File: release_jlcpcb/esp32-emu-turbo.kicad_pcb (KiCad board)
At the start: 4 copper layers, 160 x 75 mm, 71 parts, among them J1 USB-C-16P, J3 JST-PH-2P, J4 FPC-40P-0.5mm, SW1 SW-SMD-5.1x5.1, SW10 SW-SMD-5.1x5.1, SW11 SW-SMD-5.1x5.1, SW12 SW-SMD-5.1x5.1, SW13 SW-SMD-5.1x5.1, SW2 SW-SMD-5.1x5.1, SW3 SW-SMD-5.1x5.1, SW4 SW-SMD-5.1x5.1, SW5 SW-SMD-5.1x5.1, SW6 SW-SMD-5.1x5.1, SW7 SW-SMD-5.1x5.1, SW8 SW-SMD-5.1x5.1, SW9 SW-SMD-5.1x5.1, U1 ESP32-S3-WROOM-1-N16R8, U2 ESOP-8, U3 SOT-223, U5 SOP-16, U6 TF-01A

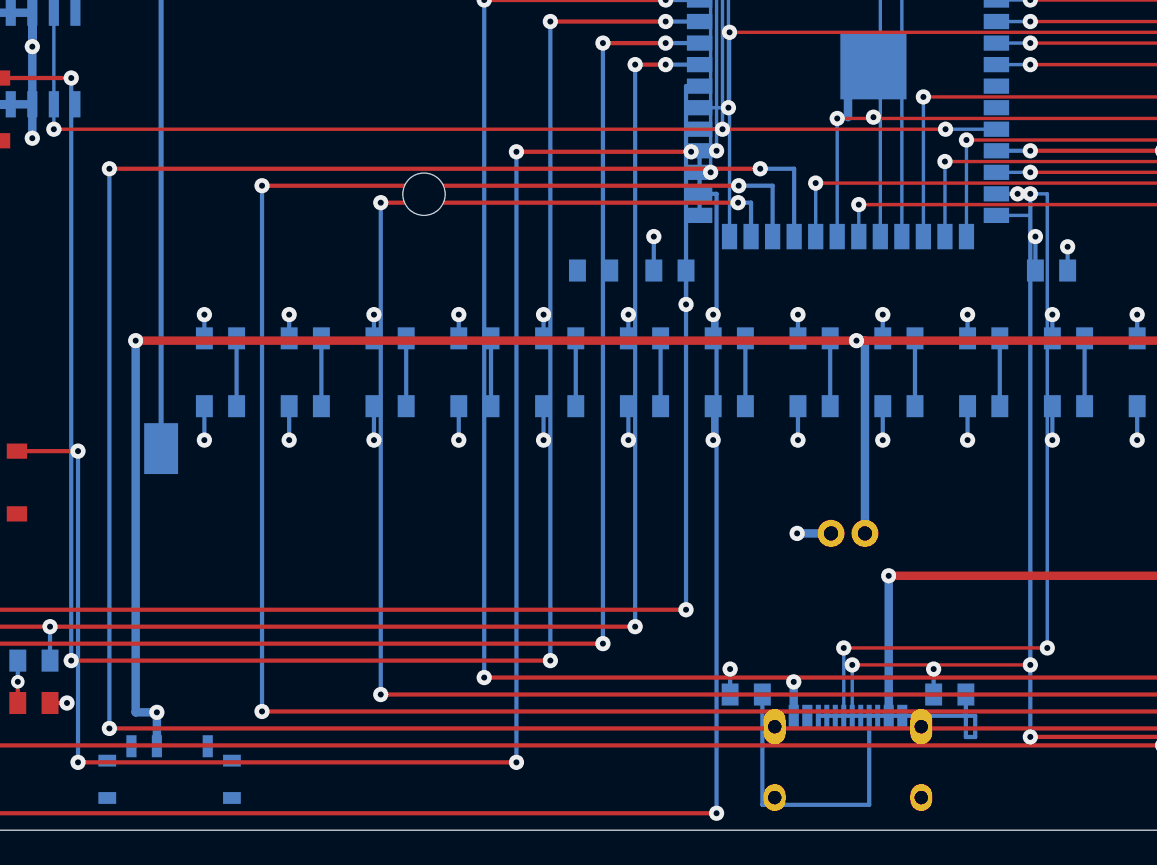
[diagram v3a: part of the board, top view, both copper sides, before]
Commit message: Fix 4 JLCPCB DFM DANGER violations: USB trace spacing, button via/MH clearance
- USB D+/D- B.Cu columns shifted inward (dp_col_x +1.5, dm_col_x +2.5) to
  clear GND cap traces (gap 0.575mm, was 0.075mm)
- Button stagger_y lowered to 35.5 (was 38.0) to clear MH(55,37.5) drill zone
- Button near_epx vias staggered with 0.4mm offset to separate BTN_B/BTN_X
  via pair (pad gap 0.177mm, was 0.101mm)
- Added 2 DFM guard tests: USB cap trace spacing + MH trace clearance (41/41)
- Regenerated gerbers with zone fill + updated release_jlcpcb + SVG renders

Co-Authored-By: Claude Opus 4.6 <noreply@anthropic.com>
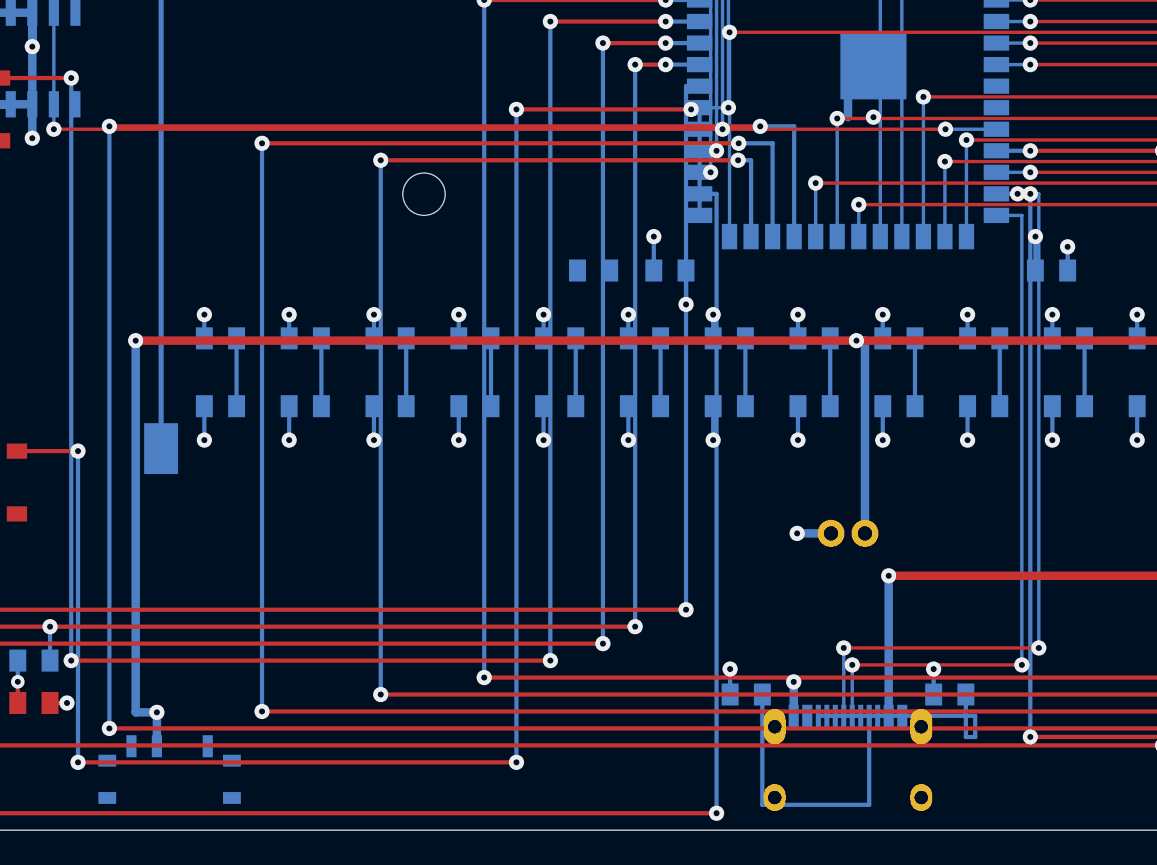
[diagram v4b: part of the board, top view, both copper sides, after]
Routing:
- net BTN_Y: track 213.9 -> 218.9 mm
- net BTN_X: track 189.0 -> 194.0 mm
- net BTN_SELECT: track 102.3 -> 107.3 mm
- net BTN_B: track 189.7 -> 194.7 mm
- net USB_D-: track 45.8 -> 44.8 mm
- net USB_D+: track 42.0 -> 41.0 mm
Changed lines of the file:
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@@
   (segment (start 80.25 68.255) (end 80.25 65.255) (width 0.2) (layer "B.Cu") (net 40))
   (via (at 80.25 65.255) (size 0.9) (drill 0.35) (layers "F.Cu" "B.Cu") (net 40))
-  (segment (start 80.25 65.255) (end 90.75 65.255) (width 0.2) (layer "F.Cu") (net 40))
-  (via (at 90.75 65.255) (size 0.9) (drill 0.35) (layers "F.Cu" "B.Cu") (net 40))
-  (segment (start 90.75 65.255) (end 90.75 38.75) (width 0.2) (layer "B.Cu") (net 40))
-  (segment (start 90.75 38.75) (end 88.75 38.75) (width 0.2) (layer "B.Cu") (net 40))
+  (segment (start 80.25 65.255) (end 90.25 65.255) (width 0.2) (layer "F.Cu") (net 40))
+  (via (at 90.25 65.255) (size 0.9) (drill 0.35) (layers "F.Cu" "B.Cu") (net 40))
+  (segment (start 90.25 65.255) (end 90.25 38.75) (width 0.2) (layer "B.Cu") (net 40))
+  (segment (start 90.25 38.75) (end 88.75 38.75) (width 0.2) (layer "B.Cu") (net 40))
   (segment (start 79.75 68.255) (end 79.75 64.255) (width 0.2) (layer "B.Cu") (net 41))
   (via (at 79.75 64.255) (size 0.9) (drill 0.35) (layers "F.Cu" "B.Cu") (net 41))
-  (segment (start 79.75 64.255) (end 91.75 64.255) (width 0.2) (layer "F.Cu") (net 41))
-  (via (at 91.75 64.255) (size 0.9) (drill 0.35) (layers "F.Cu" "B.Cu") (net 41))
-  (segment (start 91.75 64.255) (end 91.75 37.480000000000004) (width 0.2) (layer "B.Cu") (net 41))
-  (segment (start 91.75 37.480000000000004) (end 88.75 37.480000000000004) (width 0.2) (layer "B.Cu") (net 41))
+  (segment (start 79.75 64.255) (end 91.25 64.255) (width 0.2) (layer "F.Cu") (net 41))
+  (via (at 91.25 64.255) (size 0.9) (drill 0.35) (layers "F.Cu" "B.Cu") (net 41))
+  (segment (start 91.25 64.255) (end 91.25 37.480000000000004) (width 0.2) (layer "B.Cu") (net 41))
+  (segment (start 91.25 37.480000000000004) (end 88.75 37.480000000000004) (width 0.2) (layer "B.Cu") (net 41))
   (segment (start 78.25 68.255) (end 87.5 68.255) (width 0.25) (layer "B.Cu") (net 49))
   (segment (start 87.5 68.255) (end 87.5 69.505) (width 0.25) (layer "B.Cu") (net 49))
@@
   (segment (start 131.4 67.0) (end 52.45 67.0) (width 0.25) (layer "F.Cu") (net 32))
   (via (at 52.45 67.0) (size 0.9) (drill 0.35) (layers "F.Cu" "B.Cu") (net 32))
-  (segment (start 52.45 67.0) (end 52.45 38.0) (width 0.25) (layer "B.Cu") (net 32))
-  (via (at 52.45 38.0) (size 0.9) (drill 0.35) (layers "F.Cu" "B.Cu") (net 32))
-  (segment (start 52.45 38.0) (end 73.52 38.0) (width 0.25) (layer "F.Cu") (net 32))
-  (via (at 73.52 38.0) (size 0.9) (drill 0.35) (layers "F.Cu" "B.Cu") (net 32))
-  (segment (start 73.52 38.0) (end 74.285 38.0) (width 0.25) (layer "B.Cu") (net 32))
-  (segment (start 74.285 38.0) (end 74.285 40.0) (width 0.25) (layer "B.Cu") (net 32))
+  (segment (start 52.45 67.0) (end 52.45 35.5) (width 0.25) (layer "B.Cu") (net 32))
+  (via (at 52.45 35.5) (size 0.9) (drill 0.35) (layers "F.Cu" "B.Cu") (net 32))
+  (segment (start 52.45 35.5) (end 73.52 35.5) (width 0.25) (layer "F.Cu") (net 32))
+  (via (at 73.52 35.5) (size 0.9) (drill 0.35) (layers "F.Cu" "B.Cu") (net 32))
+  (segment (start 73.52 35.5) (end 74.285 35.5) (width 0.25) (layer "B.Cu") (net 32))
+  (segment (start 74.285 35.5) (end 74.285 40.0) (width 0.25) (layer "B.Cu") (net 32))
   (segment (start 155.0 34.35) (end 153.5 34.35) (width 0.25) (layer "F.Cu") (net 1))
   (segment (start 153.5 34.35) (end 153.5 34.85) (width 0.25) (layer "F.Cu") (net 1))
@@
   (segment (start 131.0 68.0) (end 45.45 68.0) (width 0.25) (layer "F.Cu") (net 33))
   (via (at 45.45 68.0) (size 0.9) (drill 0.35) (layers "F.Cu" "B.Cu") (net 33))
-  (segment (start 45.45 68.0) (end 45.45 37.0) (width 0.25) (layer "B.Cu") (net 33))
-  (via (at 45.45 37.0) (size 0.9) (drill 0.35) (layers "F.Cu" "B.Cu") (net 33))
-  (segment (start 45.45 37.0) (end 73.555 37.0) (width 0.25) (layer "F.Cu") (net 33))
-  (via (at 73.555 37.0) (size 0.9) (drill 0.35) (layers "F.Cu" "B.Cu") (net 33))
-  (segment (start 73.555 37.0) (end 75.555 37.0) (width 0.25) (layer "B.Cu") (net 33))
-  (segment (start 75.555 37.0) (end 75.555 40.0) (width 0.25) (layer "B.Cu") (net 33))
+  (segment (start 45.45 68.0) (end 45.45 34.5) (width 0.25) (layer "B.Cu") (net 33))
+  (via (at 45.45 34.5) (size 0.9) (drill 0.35) (layers "F.Cu" "B.Cu") (net 33))
+  (segment (start 45.45 34.5) (end 73.555 34.5) (width 0.25) (layer "F.Cu") (net 33))
+  (via (at 73.555 34.5) (size 0.9) (drill 0.35) (layers "F.Cu" "B.Cu") (net 33))
+  (segment (start 73.555 34.5) (end 75.555 34.5) (width 0.25) (layer "B.Cu") (net 33))
+  (segment (start 75.555 34.5) (end 75.555 40.0) (width 0.25) (layer "B.Cu") (net 33))
   (segment (start 145.0 44.35) (end 143.5 44.35) (width 0.25) (layer "F.Cu") (net 1))
   (segment (start 143.5 44.35) (end 143.5 44.85) (width 0.25) (layer "F.Cu") (net 1))
@@
   (segment (start 130.29999999999998 69.0) (end 36.45 69.0) (width 0.25) (layer "F.Cu") (net 34))
   (via (at 36.45 69.0) (size 0.9) (drill 0.35) (layers "F.Cu" "B.Cu") (net 34))
-  (segment (start 36.45 69.0) (end 36.45 36.0) (width 0.25) (layer "B.Cu") (net 34))
-  (via (at 36.45 36.0) (size 0.9) (drill 0.35) (layers "F.Cu" "B.Cu") (net 34))
-  (segment (start 36.45 36.0) (end 74.825 36.0) (width 0.25) (layer "F.Cu") (net 34))
-  (via (at 74.825 36.0) (size 0.9) (drill 0.35) (layers "F.Cu" "B.Cu") (net 34))
-  (segment (start 74.825 36.0) (end 76.825 36.0) (width 0.25) (layer "B.Cu") (net 34))
-  (segment (start 76.825 36.0) (end 76.825 40.0) (width 0.25) (layer "B.Cu") (net 34))
+  (segment (start 36.45 69.0) (end 36.45 33.5) (width 0.25) (layer "B.Cu") (net 34))
+  (via (at 36.45 33.5) (size 0.9) (drill 0.35) (layers "F.Cu" "B.Cu") (net 34))
+  (segment (start 36.45 33.5) (end 74.825 33.5) (width 0.25) (layer "F.Cu") (net 34))
+  (via (at 74.825 33.5) (size 0.9) (drill 0.35) (layers "F.Cu" "B.Cu") (net 34))
+  (segment (start 74.825 33.5) (end 76.825 33.5) (width 0.25) (layer "B.Cu") (net 34))
+  (segment (start 76.825 33.5) (end 76.825 40.0) (width 0.25) (layer "B.Cu") (net 34))
   (segment (start 136.0 34.35) (end 134.5 34.35) (width 0.25) (layer "F.Cu") (net 1))
   (segment (start 134.5 34.35) (end 134.5 34.85) (width 0.25) (layer "F.Cu") (net 1))
@@
   (segment (start 34.6 71.0) (end 60.45 71.0) (width 0.25) (layer "F.Cu") (net 36))
   (via (at 60.45 71.0) (size 0.9) (drill 0.35) (layers "F.Cu" "B.Cu") (net 36))
-  (segment (start 60.45 71.0) (end 60.45 35.0) (width 0.25) (layer "B.Cu") (net 36))
-  (via (at 60.45 35.0) (size 0.9) (drill 0.35) (layers "F.Cu" "B.Cu") (net 36))
-  (segment (start 60.45 35.0) (end 70.75 35.0) (width 0.25) (layer "F.Cu") (net 36))
-  (via (at 70.75 35.0) (size 0.9) (drill 0.35) (layers "F.Cu" "B.Cu") (net 36))
-  (segment (start 70.75 35.0) (end 71.25 35.0) (width 0.25) (layer "B.Cu") (net 36))
-  (segment (start 71.25 35.0) (end 71.25 38.75) (width 0.25) (layer "B.Cu") (net 36))
+  (segment (start 60.45 71.0) (end 60.45 32.5) (width 0.25) (layer "B.Cu") (net 36))
+  (via (at 60.45 32.5) (size 0.9) (drill 0.35) (layers "F.Cu" "B.Cu") (net 36))
+  (segment (start 60.45 32.5) (end 70.75 32.5) (width 0.25) (layer "F.Cu") (net 36))
+  (via (at 70.75 32.5) (size 0.9) (drill 0.35) (layers "F.Cu" "B.Cu") (net 36))
+  (segment (start 70.75 32.5) (end 71.25 32.5) (width 0.25) (layer "B.Cu") (net 36))
+  (segment (start 71.25 32.5) (end 71.25 38.75) (width 0.25) (layer "B.Cu") (net 36))
   (segment (start 25.0 56.35) (end 26.5 56.35) (width 0.25) (layer "F.Cu") (net 1))
   (segment (start 26.5 56.35) (end 26.5 56.85) (width 0.25) (layer "F.Cu") (net 1))

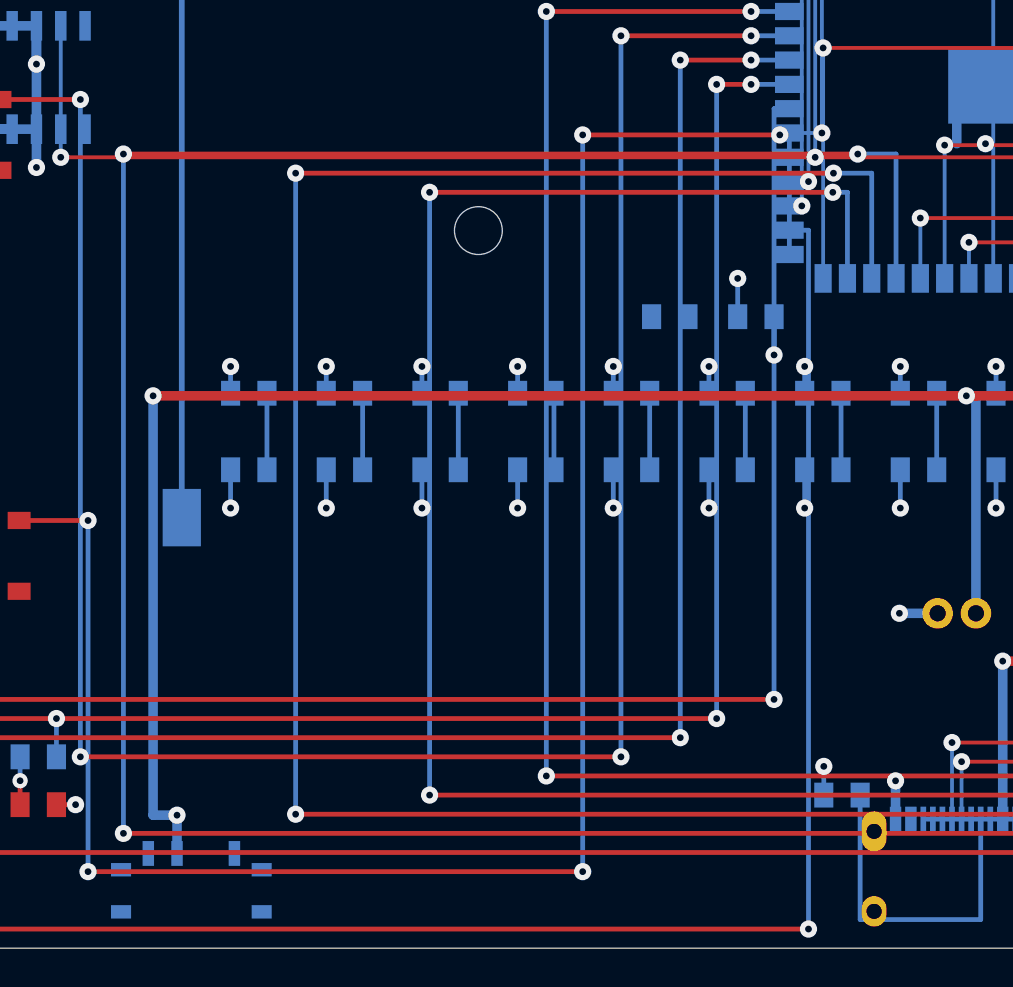
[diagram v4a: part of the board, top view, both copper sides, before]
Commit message: Fix last 2 JLCPCB DFM DANGER: button stagger via pad spacing
- Increased button stagger Y step from 1.0mm to 1.2mm to separate
  BTN_A/BTN_X via pair (pad gap 0.30mm, was 0.10mm DANGER)
- Both F.Cu and B.Cu pad spacing dangers resolved (same via pair)
- 41/41 DFM tests pass, trace spacing improved to 16 (baseline 27)
- Regenerated gerbers + release_jlcpcb + SVG renders

Co-Authored-By: Claude Opus 4.6 <noreply@anthropic.com>
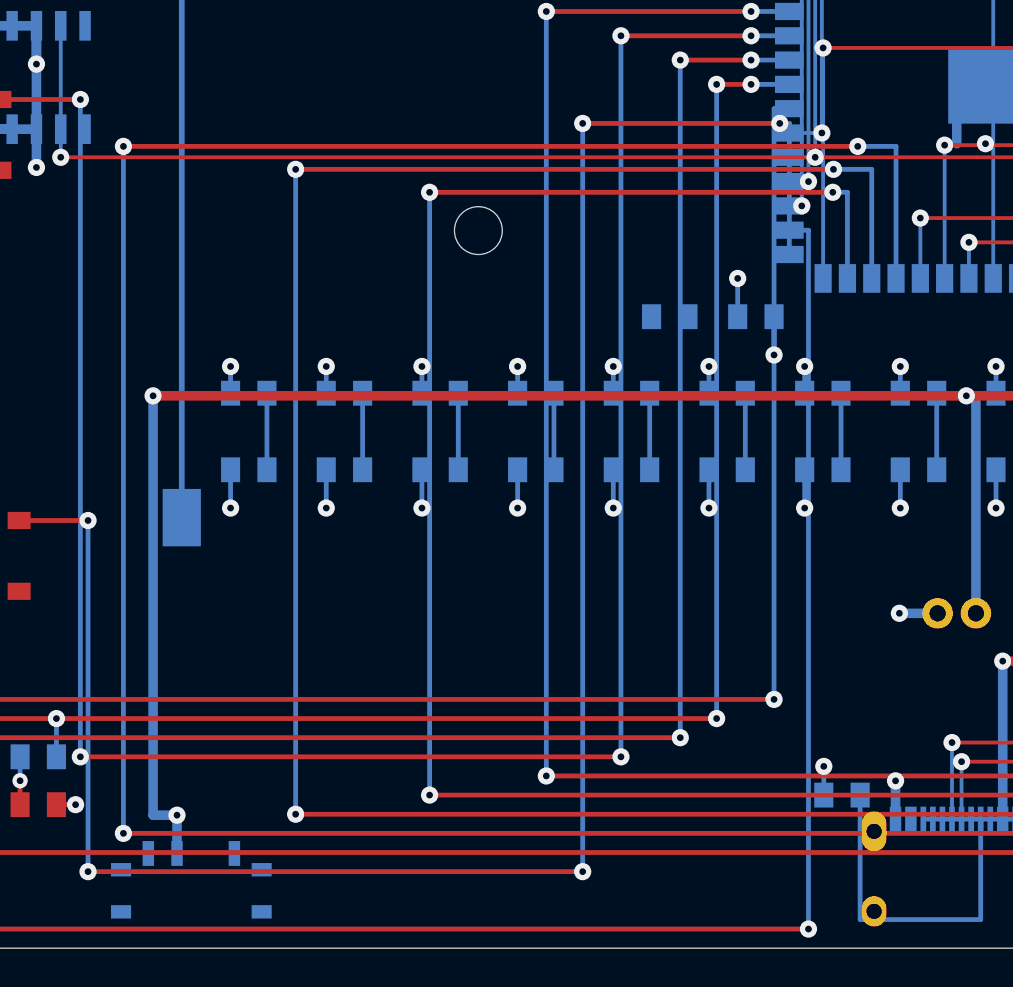
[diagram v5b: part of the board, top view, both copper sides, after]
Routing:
- net BTN_SELECT: track 107.3 -> 108.6 mm
- net BTN_Y: track 218.9 -> 219.7 mm
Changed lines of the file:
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@@
   (segment (start 131.0 68.0) (end 45.45 68.0) (width 0.25) (layer "F.Cu") (net 33))
   (via (at 45.45 68.0) (size 0.9) (drill 0.35) (layers "F.Cu" "B.Cu") (net 33))
-  (segment (start 45.45 68.0) (end 45.45 34.5) (width 0.25) (layer "B.Cu") (net 33))
-  (via (at 45.45 34.5) (size 0.9) (drill 0.35) (layers "F.Cu" "B.Cu") (net 33))
-  (segment (start 45.45 34.5) (end 73.555 34.5) (width 0.25) (layer "F.Cu") (net 33))
-  (via (at 73.555 34.5) (size 0.9) (drill 0.35) (layers "F.Cu" "B.Cu") (net 33))
-  (segment (start 73.555 34.5) (end 75.555 34.5) (width 0.25) (layer "B.Cu") (net 33))
-  (segment (start 75.555 34.5) (end 75.555 40.0) (width 0.25) (layer "B.Cu") (net 33))
+  (segment (start 45.45 68.0) (end 45.45 34.3) (width 0.25) (layer "B.Cu") (net 33))
+  (via (at 45.45 34.3) (size 0.9) (drill 0.35) (layers "F.Cu" "B.Cu") (net 33))
+  (segment (start 45.45 34.3) (end 73.555 34.3) (width 0.25) (layer "F.Cu") (net 33))
+  (via (at 73.555 34.3) (size 0.9) (drill 0.35) (layers "F.Cu" "B.Cu") (net 33))
+  (segment (start 73.555 34.3) (end 75.555 34.3) (width 0.25) (layer "B.Cu") (net 33))
+  (segment (start 75.555 34.3) (end 75.555 40.0) (width 0.25) (layer "B.Cu") (net 33))
   (segment (start 145.0 44.35) (end 143.5 44.35) (width 0.25) (layer "F.Cu") (net 1))
   (segment (start 143.5 44.35) (end 143.5 44.85) (width 0.25) (layer "F.Cu") (net 1))
@@
   (segment (start 130.29999999999998 69.0) (end 36.45 69.0) (width 0.25) (layer "F.Cu") (net 34))
   (via (at 36.45 69.0) (size 0.9) (drill 0.35) (layers "F.Cu" "B.Cu") (net 34))
-  (segment (start 36.45 69.0) (end 36.45 33.5) (width 0.25) (layer "B.Cu") (net 34))
-  (via (at 36.45 33.5) (size 0.9) (drill 0.35) (layers "F.Cu" "B.Cu") (net 34))
-  (segment (start 36.45 33.5) (end 74.825 33.5) (width 0.25) (layer "F.Cu") (net 34))
-  (via (at 74.825 33.5) (size 0.9) (drill 0.35) (layers "F.Cu" "B.Cu") (net 34))
-  (segment (start 74.825 33.5) (end 76.825 33.5) (width 0.25) (layer "B.Cu") (net 34))
-  (segment (start 76.825 33.5) (end 76.825 40.0) (width 0.25) (layer "B.Cu") (net 34))
+  (segment (start 36.45 69.0) (end 36.45 33.1) (width 0.25) (layer "B.Cu") (net 34))
+  (via (at 36.45 33.1) (size 0.9) (drill 0.35) (layers "F.Cu" "B.Cu") (net 34))
+  (segment (start 36.45 33.1) (end 74.825 33.1) (width 0.25) (layer "F.Cu") (net 34))
+  (via (at 74.825 33.1) (size 0.9) (drill 0.35) (layers "F.Cu" "B.Cu") (net 34))
+  (segment (start 74.825 33.1) (end 76.825 33.1) (width 0.25) (layer "B.Cu") (net 34))
+  (segment (start 76.825 33.1) (end 76.825 40.0) (width 0.25) (layer "B.Cu") (net 34))
   (segment (start 136.0 34.35) (end 134.5 34.35) (width 0.25) (layer "F.Cu") (net 1))
   (segment (start 134.5 34.35) (end 134.5 34.85) (width 0.25) (layer "F.Cu") (net 1))
@@
   (segment (start 34.6 71.0) (end 60.45 71.0) (width 0.25) (layer "F.Cu") (net 36))
   (via (at 60.45 71.0) (size 0.9) (drill 0.35) (layers "F.Cu" "B.Cu") (net 36))
-  (segment (start 60.45 71.0) (end 60.45 32.5) (width 0.25) (layer "B.Cu") (net 36))
-  (via (at 60.45 32.5) (size 0.9) (drill 0.35) (layers "F.Cu" "B.Cu") (net 36))
-  (segment (start 60.45 32.5) (end 70.75 32.5) (width 0.25) (layer "F.Cu") (net 36))
-  (via (at 70.75 32.5) (size 0.9) (drill 0.35) (layers "F.Cu" "B.Cu") (net 36))
-  (segment (start 70.75 32.5) (end 71.25 32.5) (width 0.25) (layer "B.Cu") (net 36))
-  (segment (start 71.25 32.5) (end 71.25 38.75) (width 0.25) (layer "B.Cu") (net 36))
+  (segment (start 60.45 71.0) (end 60.45 31.9) (width 0.25) (layer "B.Cu") (net 36))
+  (via (at 60.45 31.9) (size 0.9) (drill 0.35) (layers "F.Cu" "B.Cu") (net 36))
+  (segment (start 60.45 31.9) (end 70.75 31.9) (width 0.25) (layer "F.Cu") (net 36))
+  (via (at 70.75 31.9) (size 0.9) (drill 0.35) (layers "F.Cu" "B.Cu") (net 36))
+  (segment (start 70.75 31.9) (end 71.25 31.9) (width 0.25) (layer "B.Cu") (net 36))
+  (segment (start 71.25 31.9) (end 71.25 38.75) (width 0.25) (layer "B.Cu") (net 36))
   (segment (start 25.0 56.35) (end 26.5 56.35) (width 0.25) (layer "F.Cu") (net 1))
   (segment (start 26.5 56.35) (end 26.5 56.85) (width 0.25) (layer "F.Cu") (net 1))

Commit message: Update release_jlcpcb with v2.3 gerbers (zone fill + back silkscreen title)
Co-Authored-By: Claude Opus 4.6 <noreply@anthropic.com>
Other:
- board text added: "ESP32-EMU-TURBO CPJ&CP 2026"
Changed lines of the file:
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@@
   (gr_text "L" (at 15.0 10.5) (layer "B.Fab") (effects (font (size 0.8 0.8) (thickness 0.2)) (justify mirror)))
   (gr_text "R" (at 145.0 10.5) (layer "B.Fab") (effects (font (size 0.8 0.8) (thickness 0.2)) (justify mirror)))
+  (gr_text "ESP32-EMU-TURBO CPJ&CP 2026" (at 80.0 3.0) (layer "B.SilkS") (effects (font (size 0.8 0.8) (thickness 0.2)) (justify mirror)))
   (footprint "SW-SMD-5.1x5.1" (at 18.0 23.5) (layer "F.Cu")
     (property "Reference" "SW1" (at 0 -3 0) (layer "F.Fab") (effects (font (size 1 1) (thickness 0.2))))
